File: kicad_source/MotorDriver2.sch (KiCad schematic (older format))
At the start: 17 parts, among them P3 CONN_01X04, P4 CONN_01X05, U1 TMC5130A-TA

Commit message: generated pdf files
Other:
- note added: "Copyright generationmake 2019\nsee full project documentation at https://github.com/generationmake/StepperMotorFeatherWing"
- note removed: "Copyright generationmake 2019\nsee full project documentation at http://arduhmi.generationmake.de"
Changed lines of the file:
@@
 Sheet 5 6
 Title "HighPowerMotorFeatherWing"
-Date "2019-12-01"
+Date "2019-12-31"
 Rev "1.0"
 Comp "generationmake"
@@
 $EndDescr
 Text Notes 500  650  0    47   ~ 0
-Copyright generationmake 2019\nsee full project documentation at http://arduhmi.generationmake.de
+Copyright generationmake 2019\nsee full project documentation at https://github.com/generationmake/StepperMotorFeatherWing
 Text Notes 7000 6900 0    43   ~ 0
 You may redistribute and modify this documentation under the terms of the CERN OHL v.1.2. (http://ohwr.org/cernohl). \nThis documentation is distributed WITHOUT ANY EXPRESS OR IMPLIED WARRANTY, INCLUDING OF MERCHANTABILITY, SATISFACTORY \nQUALITY AND FITNESS FOR A PARTICULAR PURPOSE. Please see the CERN OHL v.1.2  for applicable conditions

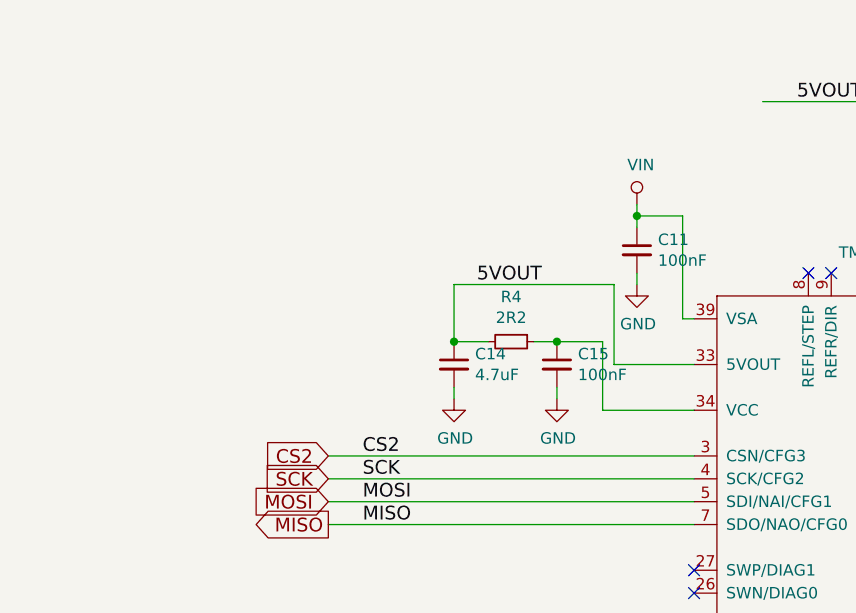
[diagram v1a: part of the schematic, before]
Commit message: added external supply for +5V for TMC5130
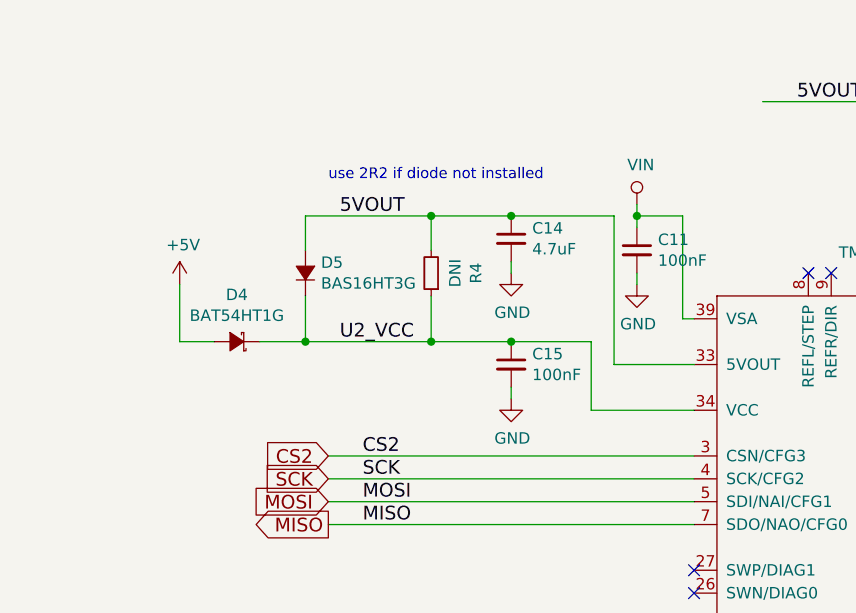
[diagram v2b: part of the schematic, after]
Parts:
- added D4: BAT54HT1G, diodes:SOD-323, symbol devices:D_Schottky_Small
- added D5: BAS16HT3G, diodes:SOD-323, symbol devices:D_Small
- R4: value 2R2 -> DNI
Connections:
- net 5VOUT: now also D5.2 (A)
- net U2_VCC: now reaches C15.1, R4.1, U1.34 (VCC)
- net U2_VCC: now also D4.1 (K), D5.1 (K)
- new net +5V: D4.2 (A)
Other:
- note added: "use 2R2 if diode not installed"
- moved on the sheet: C14, C15, R4
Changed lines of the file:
@@
 L devices:C_0603 C15
 U 1 1 5DED18D9
-P 4450 2450
-F 0 "C15" H 4542 2496 50  0000 L CNN
-F 1 "100nF" H 4542 2405 50  0000 L CNN
-F 2 "capacitors:C_0603" H 4450 2300 50  0001 C CNN
-F 3 "" H 4450 2450 50  0000 C CNN
-	1    4450 2450
+P 4250 2450
+F 0 "C15" H 4342 2496 50  0000 L CNN
+F 1 "100nF" H 4342 2405 50  0000 L CNN
+F 2 "capacitors:C_0603" H 4250 2300 50  0001 C CNN
+F 3 "" H 4250 2450 50  0000 C CNN
+	1    4250 2450
 	1    0    0    -1
 $EndComp
@@
 L devices:C_0603 C14
 U 1 1 5DF41702
-P 4000 2450
-F 0 "C14" H 4092 2496 50  0000 L CNN
-F 1 "4.7uF" H 4092 2405 50  0000 L CNN
-F 2 "capacitors:C_0603" H 4000 2300 50  0001 C CNN
-F 3 "" H 4000 2450 50  0000 C CNN
-	1    4000 2450
+P 4250 1900
+F 0 "C14" H 4342 1946 50  0000 L CNN
+F 1 "4.7uF" H 4342 1855 50  0000 L CNN
+F 2 "capacitors:C_0603" H 4250 1750 50  0001 C CNN
+F 3 "" H 4250 1900 50  0000 C CNN
+	1    4250 1900
 	1    0    0    -1
 $EndComp
@@
 L devices:R_0603 R4
 U 1 1 5DF425BD
-P 4250 2350
-F 0 "R4" V 4054 2350 50  0000 C CNN
-F 1 "2R2" V 4145 2350 50  0000 C CNN
-F 2 "resistors:R_0603" H 4250 2200 50  0001 C CNN
-F 3 "" H 4250 2350 50  0000 C CNN
-	1    4250 2350
-	0    1    1    0
-$EndComp
-$Comp
-L power-supply:GND #PWR023
-U 1 1 5DF430A5
-P 4450 2600
-F 0 "#PWR023" H 4450 2350 50  0001 C CNN
-F 1 "GND" H 4455 2427 50  0000 C CNN
-F 2 "" H 4450 2600 50  0000 C CNN
-F 3 "" H 4450 2600 50  0000 C CNN
-	1    4450 2600
-	1    0    0    -1
-$EndComp
-$Comp
-L power-supply:GND #PWR022
-U 1 1 5DF4357A
-P 4000 2600
-F 0 "#PWR022" H 4000 2350 50  0001 C CNN
-F 1 "GND" H 4005 2427 50  0000 C CNN
-F 2 "" H 4000 2600 50  0000 C CNN
-F 3 "" H 4000 2600 50  0000 C CNN
-	1    4000 2600
-	1    0    0    -1
-$EndComp
-$Comp
-L power-supply:GND #PWR019
-U 1 1 5DF4380F
-P 4800 2100
-F 0 "#PWR019" H 4800 1850 50  0001 C CNN
-F 1 "GND" H 4805 1927 50  0000 C CNN
-F 2 "" H 4800 2100 50  0000 C CNN
-F 3 "" H 4800 2100 50  0000 C CNN
-	1    4800 2100
-	1    0    0    -1
-$EndComp
-$Comp
-L power-supply:VIN #PWR017
-U 1 1 5DED18E0
-P 4800 1750
-F 0 "#PWR017" H 4800 1600 50  0001 C CNN
-F 1 "VIN" H 4817 1923 50  0000 C CNN
-F 2 "" H 4800 1750 50  0000 C CNN
-F 3 "" H 4800 1750 50  0000 C CNN
-	1    4800 1750
-	1    0    0    -1
-$EndComp
-Wire Wire Line
-	4800 1850 4800 1800
-Wire Wire Line
-	4800 2050 4800 2100
-Wire Wire Line
-	5050 2250 5000 2250
-Wire Wire Line
-	5000 2250 5000 1800
-Wire Wire Line
-	5000 1800 4800 1800
-Connection ~ 4800 1800
-Wire Wire Line
-	4800 1800 4800 1750
-Wire Wire Line
-	5050 2650 4650 2650
-Wire Wire Line
-	4650 2650 4650 2350
-Wire Wire Line
-	4650 2350 4450 2350
-Wire Wire Line
-	4450 2350 4350 2350
-Connection ~ 4450 2350
-Wire Wire Line
-	5050 2450 4700 2450
-Wire Wire Line
-	4700 2450 4700 2100
-Wire Wire Line
-	4700 2100 4000 2100
-Wire Wire Line
-	4000 2100 4000 2350
-Wire Wire Line
-	4000 2350 4150 2350
-Connection ~ 4000 2350
-Wire Wire Line
-	4000 2550 4000 2600
-Wire Wire Line
-	4450 2550 4450 2600
+P 3900 2050
+F 0 "R4" V 3704 2050 50  0000 C CNN
+F 1 "DNI" V 3795 2050 50  0000 C CNN
+F 2 "resistors:R_0603" H 3900 1900 50  0001 C CNN
+F 3 "" H 3900 2050 50  0000 C CNN
+	1    3900 2050
+	-1   0    0    1
+$EndComp
 Wire Wire Line
 	5050 3850 4950 3850
@@
 Text Label 6350 6000 0    60   ~ 0
 ENCN
-Text Label 4100 2100 0    60   ~ 0
-5VOUT
 $Comp
 L devices:R_0603 R3
@@
 Text Label 7600 3250 0    60   ~ 0
 OB2
+$Comp
+L power-supply:GND #PWR?
+U 1 1 5F06D6BC
+P 4250 2600
+AR Path="/5DEC41AF/5F06D6BC" Ref="#PWR?"  Part="1"
+AR Path="/5DE3616E/5F06D6BC" Ref="#PWR091"  Part="1"
+F 0 "#PWR091" H 4250 2350 50  0001 C CNN
+F 1 "GND" H 4255 2427 50  0000 C CNN
+F 2 "" H 4250 2600 50  0000 C CNN
+F 3 "" H 4250 2600 50  0000 C CNN
+	1    4250 2600
+	1    0    0    -1
+$EndComp
+$Comp
+L power-supply:GND #PWR?
+U 1 1 5F06D6C2
+P 4250 2050
+AR Path="/5DEC41AF/5F06D6C2" Ref="#PWR?"  Part="1"
+AR Path="/5DE3616E/5F06D6C2" Ref="#PWR090"  Part="1"
+F 0 "#PWR090" H 4250 1800 50  0001 C CNN
+F 1 "GND" H 4255 1877 50  0000 C CNN
+F 2 "" H 4250 2050 50  0000 C CNN
+F 3 "" H 4250 2050 50  0000 C CNN
+	1    4250 2050
+	1    0    0    -1
+$EndComp
+$Comp
+L power-supply:GND #PWR?
+U 1 1 5F06D6C8
+P 4800 2100
+AR Path="/5DEC41AF/5F06D6C8" Ref="#PWR?"  Part="1"
+AR Path="/5DE3616E/5F06D6C8" Ref="#PWR093"  Part="1"
+F 0 "#PWR093" H 4800 1850 50  0001 C CNN
+F 1 "GND" H 4805 1927 50  0000 C CNN
+F 2 "" H 4800 2100 50  0000 C CNN
+F 3 "" H 4800 2100 50  0000 C CNN
+	1    4800 2100
+	1    0    0    -1
+$EndComp
+$Comp
+L power-supply:VIN #PWR?
+U 1 1 5F06D6CE
+P 4800 1750
+AR Path="/5DEC41AF/5F06D6CE" Ref="#PWR?"  Part="1"
+AR Path="/5DE3616E/5F06D6CE" Ref="#PWR092"  Part="1"
+F 0 "#PWR092" H 4800 1600 50  0001 C CNN
+F 1 "VIN" H 4817 1923 50  0000 C CNN
+F 2 "" H 4800 1750 50  0000 C CNN
+F 3 "" H 4800 1750 50  0000 C CNN
+	1    4800 1750
+	1    0    0    -1
+$EndComp
+Wire Wire Line
+	4800 1850 4800 1800
+Wire Wire Line
+	4800 2050 4800 2100
+Wire Wire Line
+	5050 2250 5000 2250
+Wire Wire Line
+	5000 2250 5000 1800
+Wire Wire Line
+	5000 1800 4800 1800
+Connection ~ 4800 1800
+Wire Wire Line
+	4800 1800 4800 1750
+Wire Wire Line
+	5050 2450 4700 2450
+Wire Wire Line
+	4250 2000 4250 2050
+Wire Wire Line
+	4250 2550 4250 2600
+Text Label 3500 1800 0    60   ~ 0
+5VOUT
+Wire Wire Line
+	4600 2650 4600 2350
+Wire Wire Line
+	4600 2650 5050 2650
+Wire Wire Line
+	4700 1800 4700 2450
+Text Notes 3450 1650 0    47   ~ 0
+use 2R2 if diode not installed
+$Comp
+L devices:D_Small D?
+U 1 1 5F06D6E5
+P 3350 2050
+AR Path="/5DEC41AF/5F06D6E5" Ref="D?"  Part="1"
+AR Path="/5DE3616E/5F06D6E5" Ref="D5"  Part="1"
+F 0 "D5" V 3396 1982 50  0000 R CNN
+F 1 "BAS16HT3G" V 3305 1982 50  0000 R CNN
+F 2 "diodes:SOD-323" V 3350 2050 50  0001 C CNN
+F 3 "" V 3350 2050 50  0000 C CNN
+	1    3350 2050
+	0    -1   -1   0
+$EndComp
+$Comp
+L devices:D_Schottky_Small D?
+U 1 1 5F06D6EB
+P 3050 2350
+AR Path="/5DEC41AF/5F06D6EB" Ref="D?"  Part="1"
+AR Path="/5DE3616E/5F06D6EB" Ref="D4"  Part="1"
+F 0 "D4" H 3050 2145 50  0000 C CNN
+F 1 "BAT54HT1G" H 3050 2236 50  0000 C CNN
+F 2 "diodes:SOD-323" V 3050 2350 50  0001 C CNN
+F 3 "" V 3050 2350 50  0000 C CNN
+	1    3050 2350
+	-1   0    0    1
+$EndComp
+$Comp
+L power-supply:+5V #PWR?
+U 1 1 5F06D6F1
+P 2800 2100
+AR Path="/5DEC41AF/5F06D6F1" Ref="#PWR?"  Part="1"
+AR Path="/5DE3616E/5F06D6F1" Ref="#PWR089"  Part="1"
+F 0 "#PWR089" H 2800 1950 50  0001 C CNN
+F 1 "+5V" H 2815 2273 50  0000 C CNN
+F 2 "" H 2800 2100 50  0000 C CNN
+F 3 "" H 2800 2100 50  0000 C CNN
+	1    2800 2100
+	1    0    0    -1
+$EndComp
+Wire Wire Line
+	3150 2350 3350 2350
+Wire Wire Line
+	3350 1800 3350 1950
+Wire Wire Line
+	3350 2150 3350 2350
+Connection ~ 3350 2350
+Wire Wire Line
+	3350 2350 3900 2350
+Wire Wire Line
+	3900 2150 3900 2350
+Connection ~ 3900 2350
+Wire Wire Line
+	3900 1950 3900 1800
+Connection ~ 3900 1800
+Wire Wire Line
+	3900 1800 3350 1800
+Wire Wire Line
+	2950 2350 2800 2350
+Wire Wire Line
+	2800 2350 2800 2100
+Text Label 3500 2350 0    60   ~ 0
+U2_VCC
+Wire Wire Line
+	3900 1800 4250 1800
+Wire Wire Line
+	3900 2350 4250 2350
+Connection ~ 4250 2350
+Wire Wire Line
+	4250 2350 4600 2350
+Connection ~ 4250 1800
+Wire Wire Line
+	4250 1800 4700 1800
 $EndSCHEMATC

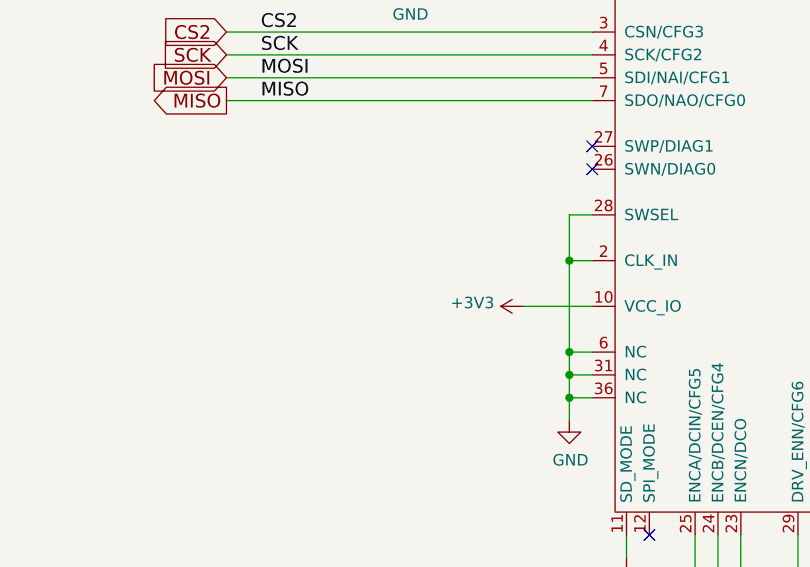
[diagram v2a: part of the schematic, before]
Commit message: added clock generator as common clock for both stepper drivers
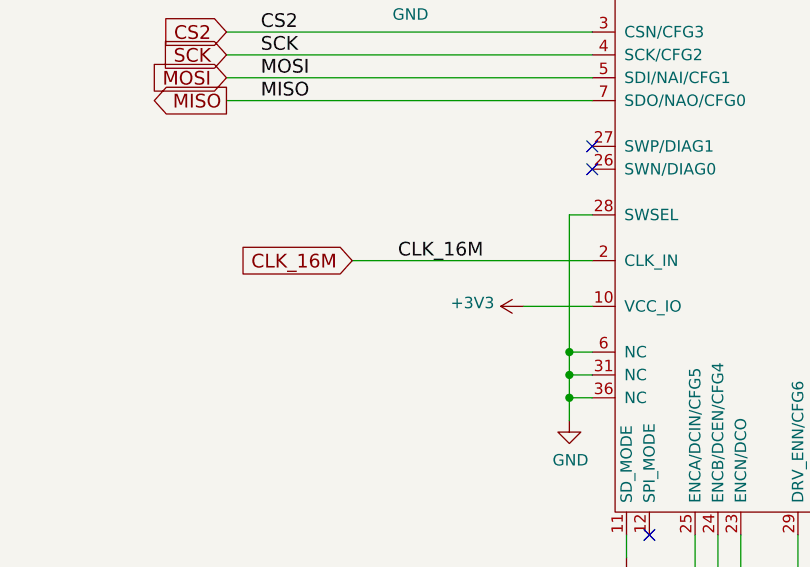
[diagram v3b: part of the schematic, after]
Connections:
- net GND: no longer U1.2 (CLK_IN)
- new net CLK_16M: U1.2 (CLK_IN)
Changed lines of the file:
@@
 	-1   0    0    1
 $EndComp
-Wire Wire Line
-	5050 3850 4950 3850
-Wire Wire Line
-	4950 3850 4950 4250
 Connection ~ 4950 4250
 $Comp
@@
 Wire Wire Line
 	5050 3650 4950 3650
-Wire Wire Line
-	4950 3650 4950 3850
-Connection ~ 4950 3850
 $Comp
 L power-supply:GND #PWR029
@@
 Wire Wire Line
 	4250 1800 4700 1800
+Wire Wire Line
+	4950 3650 4950 4250
+Text GLabel 4000 3850 0    60   Input ~ 0
+CLK_16M
+Wire Wire Line
+	5050 3850 4000 3850
+Text Label 4200 3850 0    60   ~ 0
+CLK_16M
 $EndSCHEMATC

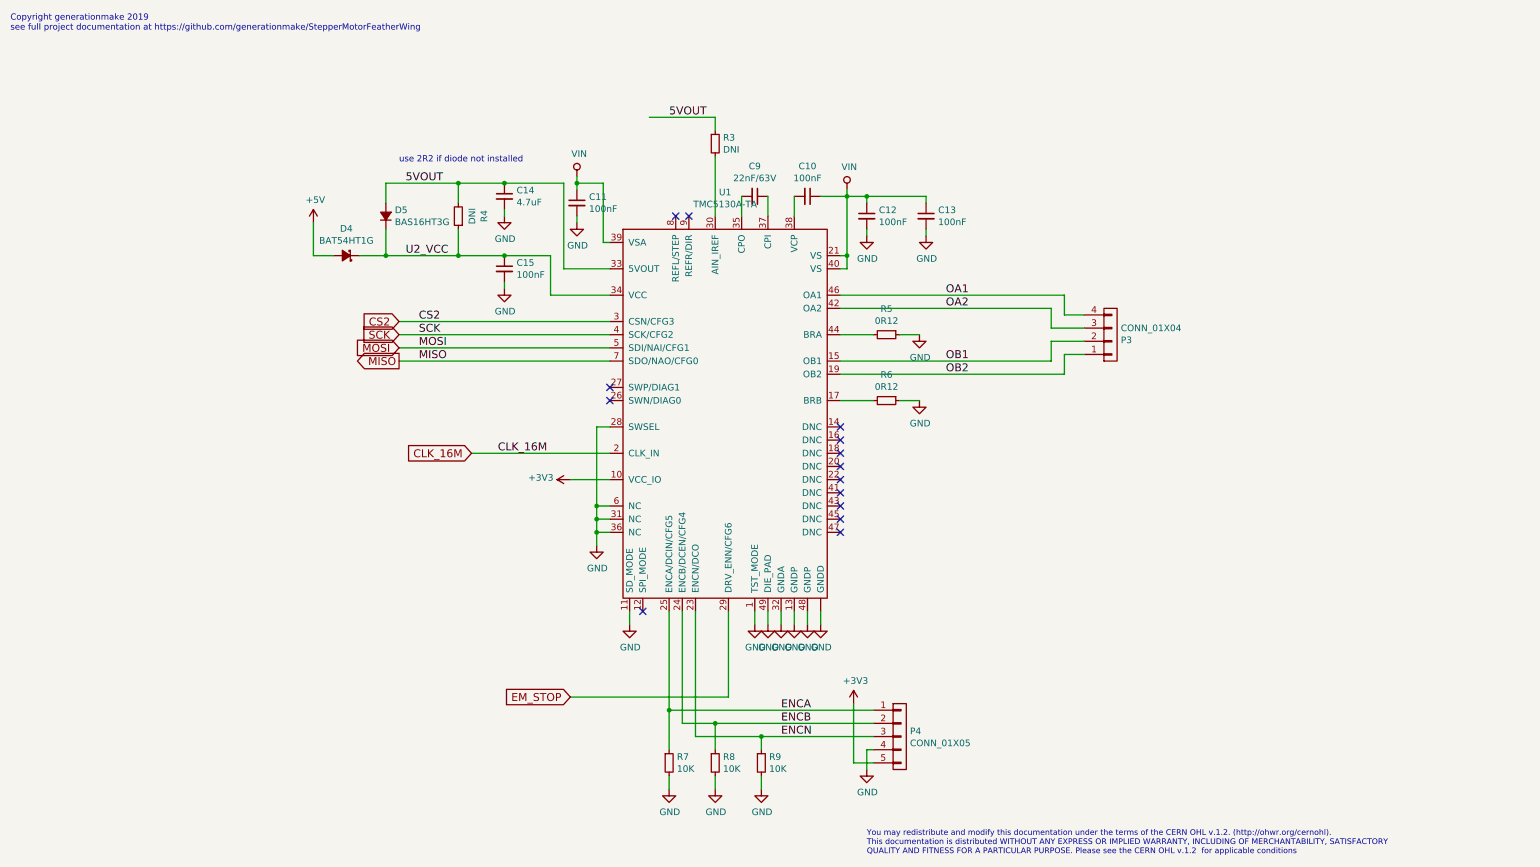
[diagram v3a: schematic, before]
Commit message: added leds and decoupling capacitors
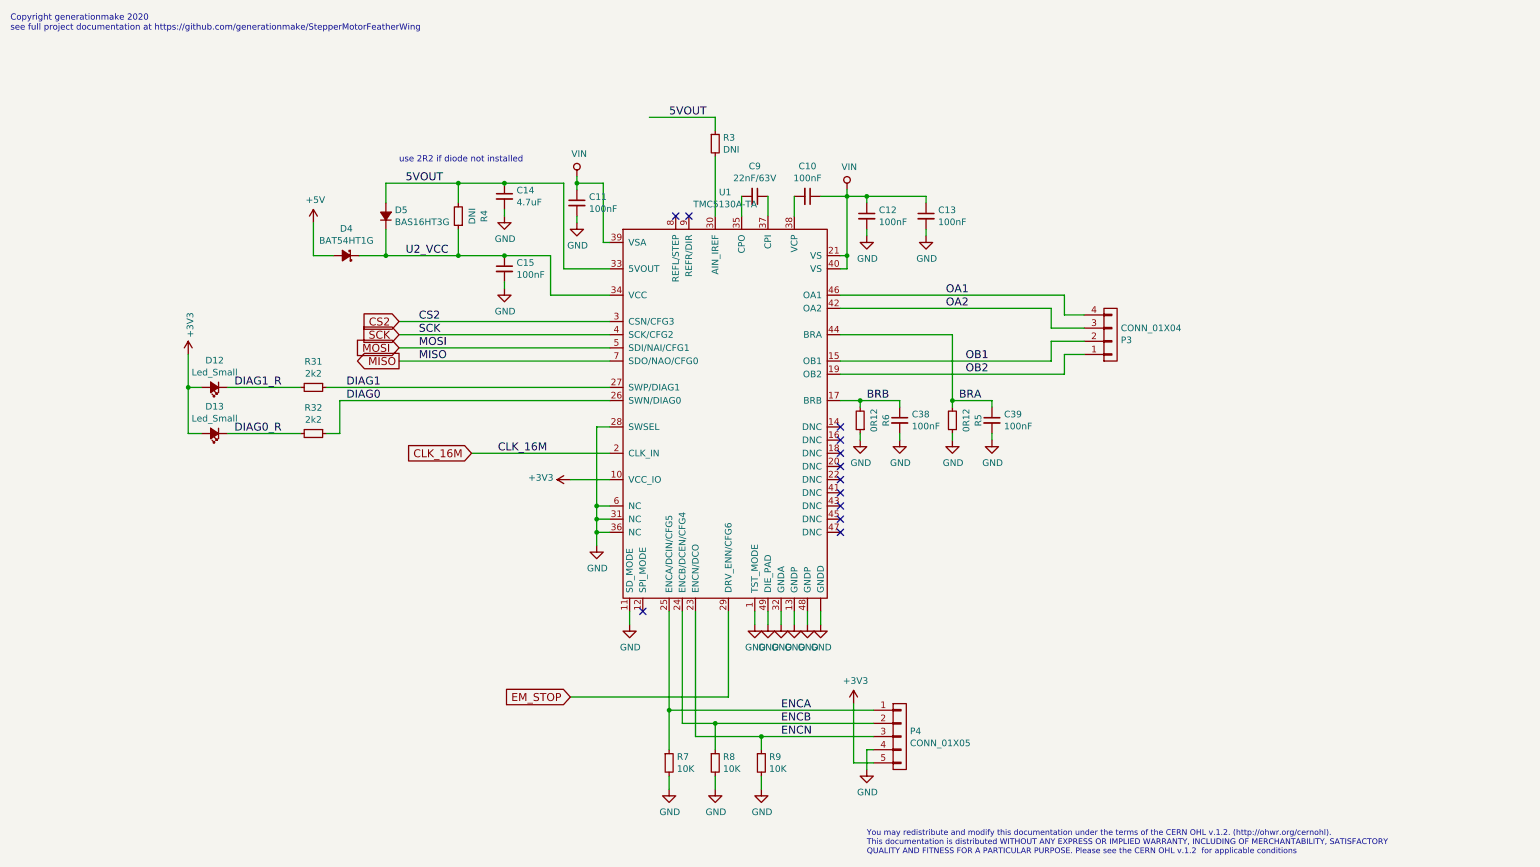
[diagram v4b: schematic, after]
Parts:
- added C38, C39: 100nF, capacitors:C_0603, symbol devices:C_0603
- added D12, D13: Led_Small, LEDs:LED_0603, symbol devices:Led_Small
- added R31, R32: 2k2, resistors:R_0603, symbol devices:R_0603
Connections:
- net +3V3: now also D12.2 (A), D13.2 (A)
- net GND: now also C38.2, C39.2
- net BRB: now reaches R6.2, U1.17 (BRB)
- net BRB: now also C38.1
- net DIAG0: now reaches U1.26 (SWN/DIAG0)
- net DIAG0: now also R32.1
- net DIAG1: now reaches U1.27 (SWP/DIAG1)
- net DIAG1: now also R31.1
- net BRA: now reaches R5.2, U1.44 (BRA)
- net BRA: now also C39.1
- new net DIAG0_R: D13.1 (K), R32.2
- new net DIAG1_R: D12.1 (K), R31.2
- no-connect marks 14 -> 12
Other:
- note added: "Copyright generationmake 2020\nsee full project documentation at https://github.com/generationmake/StepperMotorFeatherWing"
- note removed: "Copyright generationmake 2019\nsee full project documentation at https://github.com/generationmake/StepperMotorFeatherWing"
- moved on the sheet: R5, R6
